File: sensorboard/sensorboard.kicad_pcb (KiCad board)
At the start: 4 copper layers, 100 x 50 mm, 244 parts, among them J1 Conn_01x03, J10 Conn_01x02_Male, J11 Conn_01x05_Male, J12 Conn_01x03, J13 Conn_01x03, J14 USB_C_Receptacle_USB2.0, J2 Conn_01x03, J3 Conn_01x03, J4 Conn_01x03, J5 Conn_01x03, J6 Conn_01x03, J7 Conn_01x03, J8 Conn_01x03, J9 Conn_01x02_Male, Q1 MMDT2222A, U1 ESP32-PICO-D4, U10 MAX31856, U11 MAX31856, U12 RT9025-25GSP, U13 ADS1219, U14 ADS1219, U15 ADS1219, U16 MAX31856, U17 MAX31856, U18 MAX31856, U19 LTC4411, U2 LTC4411, U20 SN65HVD230, U3 TPS61092RSAR, U4 MAX31856, U5 MAX31856, U6 MAX31856, U7 MAX31856, U8 CP2102-GMR-QFN28, U9 MAX31856

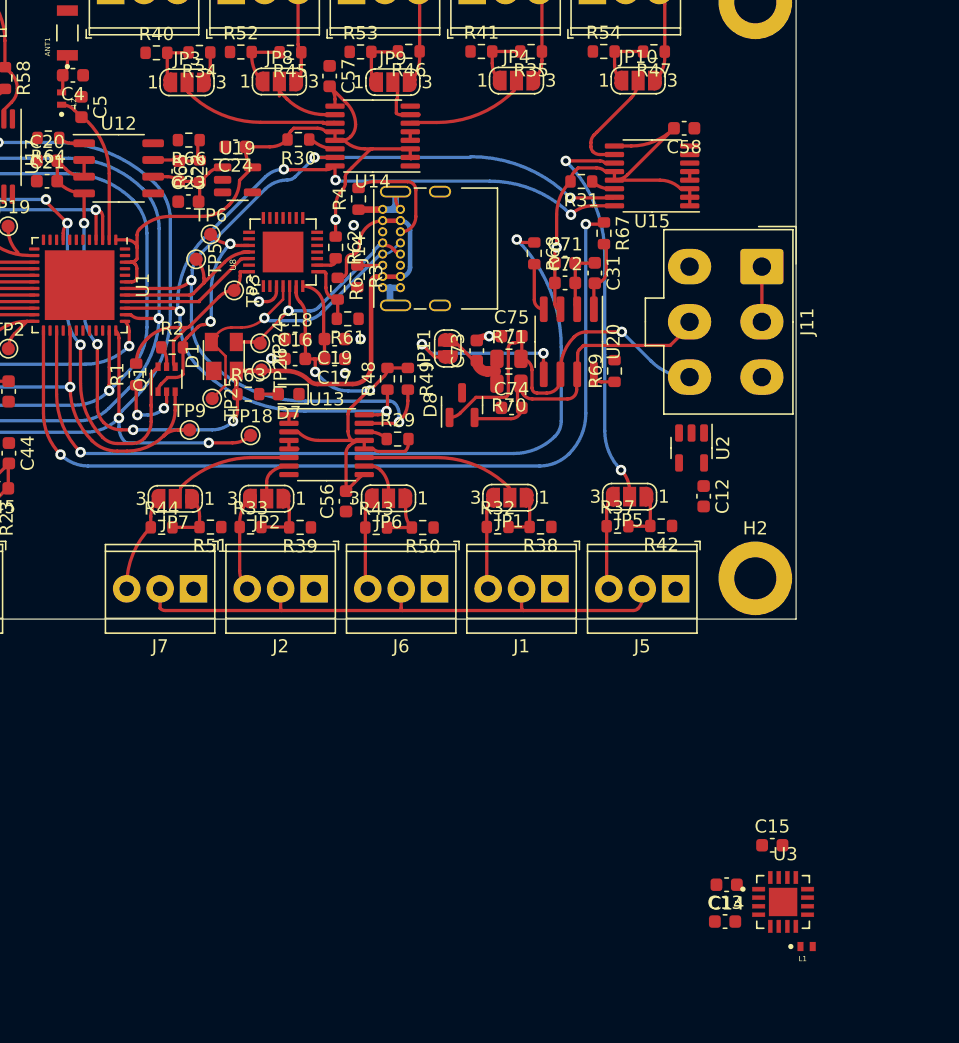
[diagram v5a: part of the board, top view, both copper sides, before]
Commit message: rearrange CAN, USB port and new copies
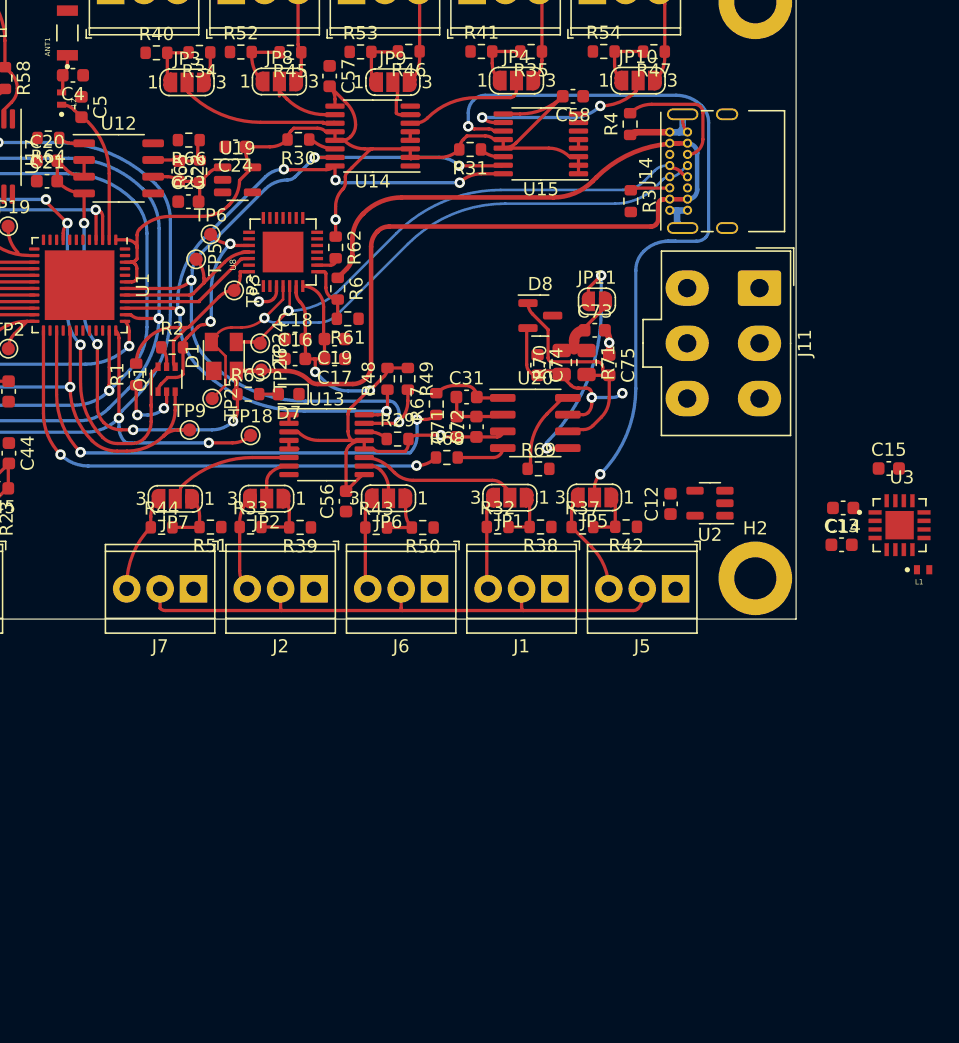
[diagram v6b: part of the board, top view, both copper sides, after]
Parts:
- moved C13 30.0 mm to (203.5, 74.3)
- moved C14 30.0 mm to (203.6, 71.5)
- moved C15 30.0 mm to (207.1, 68.5)
- moved U3 30.0 mm to (207.9, 72.9)
- moved L1 30.0 mm to (209.7, 76.2)
- moved J14 22.6 mm to (190.4, 48.9)
- moved R3 21.6 mm to (187.4, 48.2)
- moved R4 21.4 mm to (187.4, 42.4)
- moved R67 18.2 mm to (172.6, 63.6), turned to 90 degrees
- moved R68 16.9 mm to (173.4, 67.7), turned to 0 degrees
- moved C71 14.9 mm to (174.2, 65.4), turned to 90 degrees
- moved C31 13.6 mm to (174.9, 63.1), turned to 0 degrees
- moved C72 12.8 mm to (175.7, 65.4), turned to 90 degrees
- moved JP11 11.9 mm to (184.9, 55.8), turned to 0 degrees
- moved R69 9.42 mm to (180.4, 68.6), turned to 0 degrees
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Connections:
- TP22 pad 1: /CAN_TX -> /CAN_RX
- TP23 pad 1: /CAN_RX -> /CAN_TX
- U1 pad 25: /CAN_TX -> /CAN_RX
- U1 pad 27: /CAN_RX -> /CAN_TX
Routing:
- net VBUS: track 71.8 -> 123.4 mm
- net /CAN_TX: track 68.1 -> 39.3 mm
- net /analogueI2C/AIN8: track 30.5 -> 58.6 mm
- net /CAN_RX: track 63.5 -> 38.7 mm
- net /usb/Data+: track 24.8 -> 49.3 mm
- net /usb/Data-: track 19.4 -> 42.2 mm
- net /CAN_LOW: track 30.6 -> 18.5 mm, vias 1 -> 0
- net /CAN_HIGH: track 22.7 -> 13.4 mm, vias 0 -> 2
- net /SDA: track 72.4 -> 63.3 mm
- net /SCL: track 69.0 -> 60.0 mm
- net /analogueI2C/AIN9: track 8.49 -> 13.9 mm, vias 0 -> 2
- net Net-(R69-Pad1): track 1.88 -> 6.64 mm
- net /CAN/Vref: track 13.5 -> 17.7 mm
- net GND: track 25.5 -> 21.6 mm, vias 6 -> 2
- net Net-(J5-Pad3): track 7.16 -> 8.45 mm
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
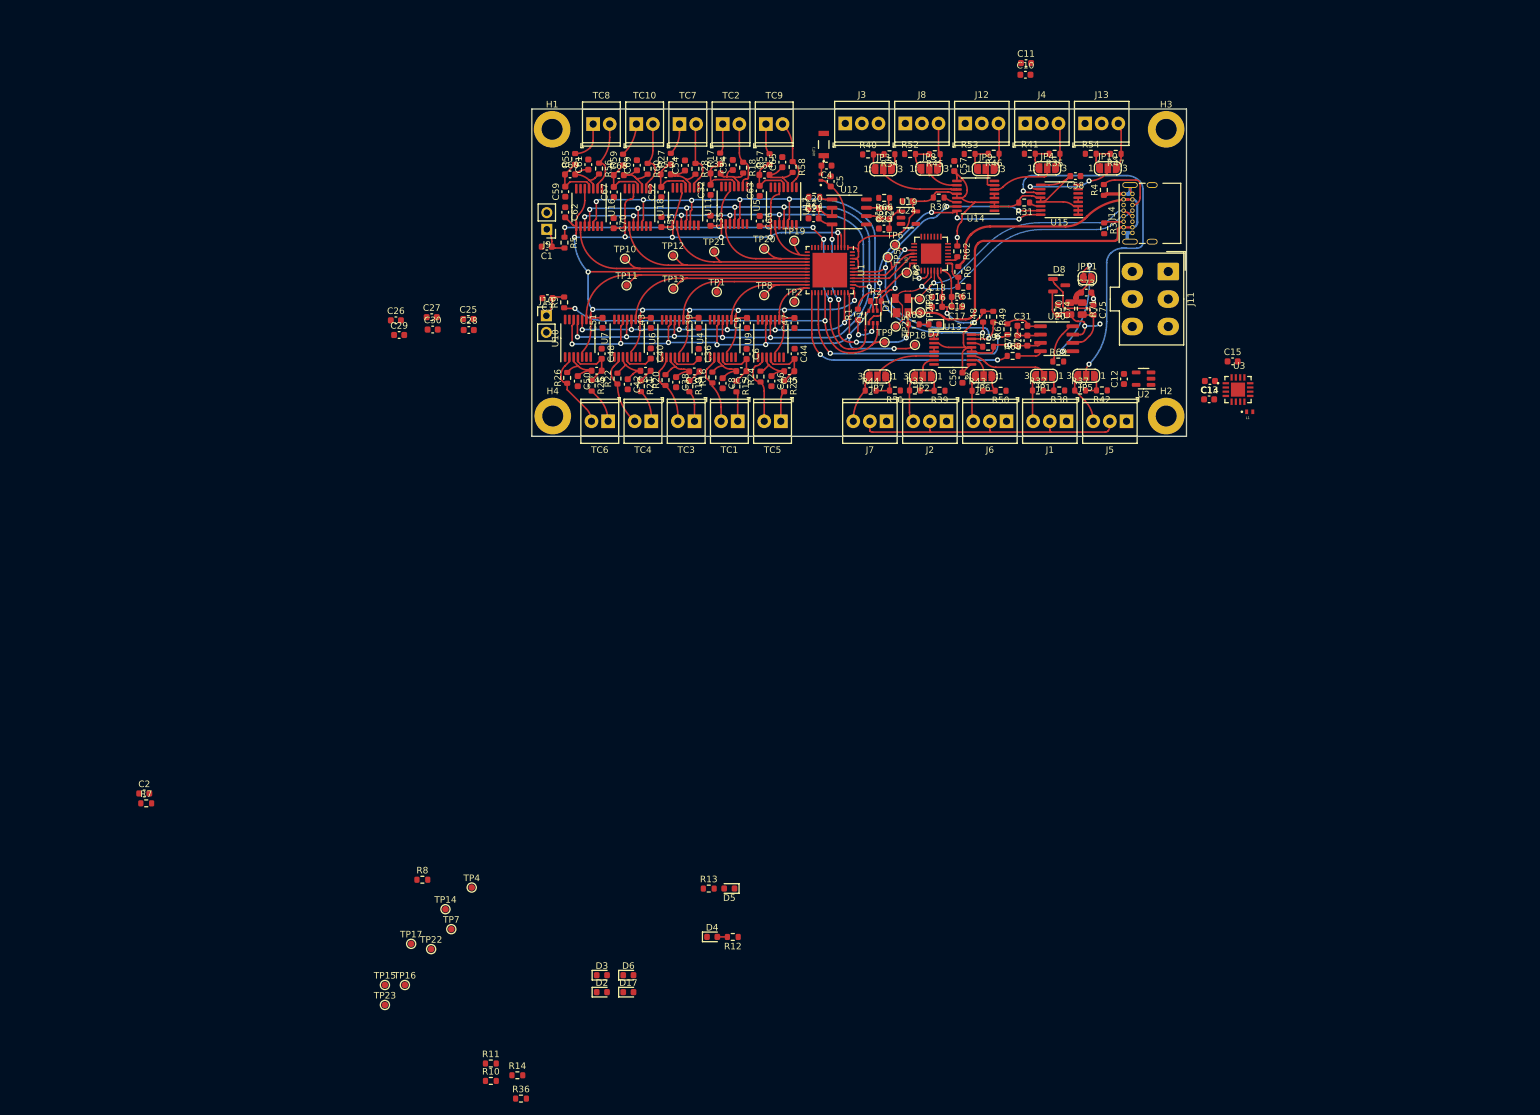
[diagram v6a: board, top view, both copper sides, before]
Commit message: LEDs and repositioning for 5V
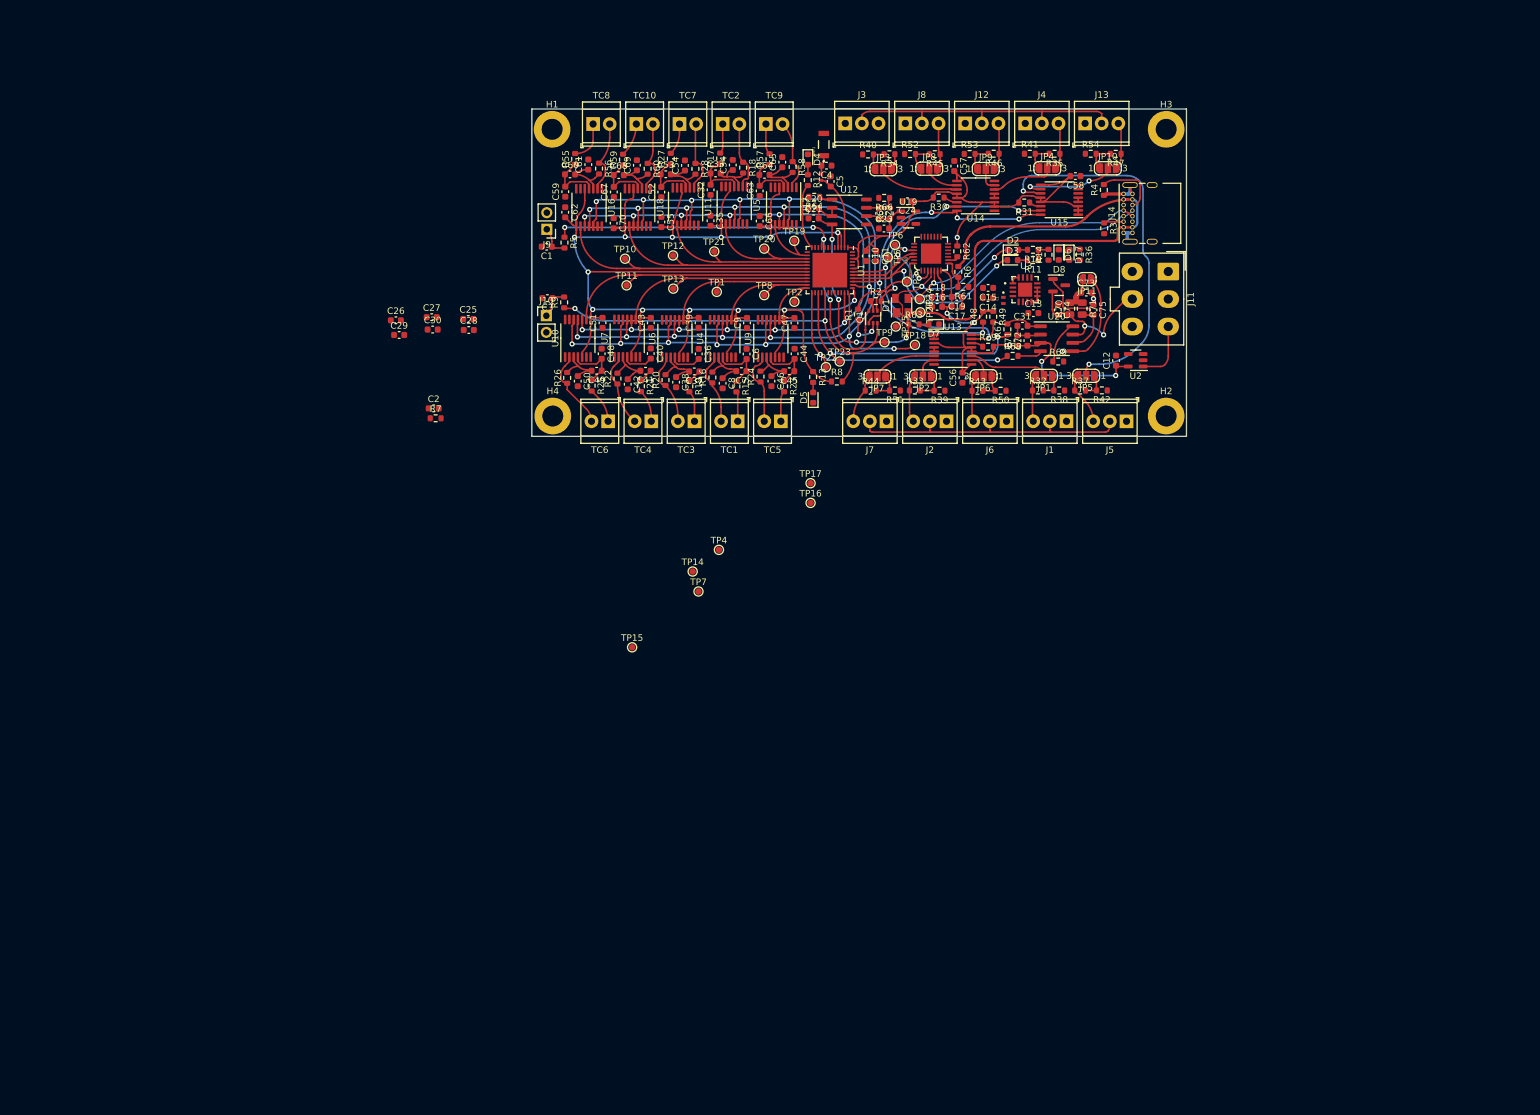
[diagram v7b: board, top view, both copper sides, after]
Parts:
- moved R36 154.6 mm to (183.7, 52.2), turned to -90 degrees
- moved R10 151.6 mm to (176.5, 51.5), turned to 180 degrees
- moved R14 149.3 mm to (178.9, 52.3), turned to 90 degrees
- moved R11 148.0 mm to (176.5, 53.1), turned to 180 degrees
- moved D17 131.2 mm to (182.1, 52.3), turned to -90 degrees
- moved D2 129.6 mm to (173.5, 51.5)
- moved D6 128.2 mm to (180.5, 52.3), turned to -90 degrees
- moved D3 126.0 mm to (173.4, 53.1)
- moved TP23 120.4 mm to (147.0, 68.6)
- moved D4 119.6 mm to (142.2, 37.7), turned to -90 degrees
- moved R12 116.2 mm to (142.2, 40.9), turned to 90 degrees
- moved TP22 107.4 mm to (144.9, 69.4)
- moved R8 99.0 mm to (146.6, 71.6)
- moved TP16 96.2 mm to (142.6, 90.2)
- moved TP17 93.1 mm to (142.6, 87.2)
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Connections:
- C13 pad 1: unconnected-(C13-Pad1) -> +3V3
- C15 pad 1: unconnected-(C15-Pad1) -> +5V
- U1 pad 12: unconnected-(U1-Pad12) -> /LED
- U1 pad 34: /LED -> unconnected-(U1-Pad34)
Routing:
- net +3V3: track 353.8 -> 402.3 mm, vias 17 -> 19
- net +5V: track 44.5 -> 91.2 mm
- net /RXD: track 13.1 -> 38.2 mm, vias 0 -> 2
- net /TXD: track 10.7 -> 34.3 mm, vias 0 -> 2
- net /LED: track 0.00 -> 10.0 mm
- net Net-(J11-Pad3): track 0.00 -> 9.34 mm
- net /CAN_HIGH: track 13.4 -> 21.7 mm
- net /BOOT: track 60.8 -> 65.6 mm
- net GND: track 21.6 -> 24.6 mm
- net /CAN_RX: track 38.7 -> 40.9 mm
- net /CAN_TX: track 39.3 -> 41.2 mm
- net /RTS: track 17.1 -> 19.0 mm
- net /CAN/Vref: track 17.7 -> 15.9 mm, vias 2 -> 1
- net Net-(D5-Pad2): track 0.00 -> 1.54 mm
- net Net-(D3-Pad2): track 0.00 -> 1.51 mm
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
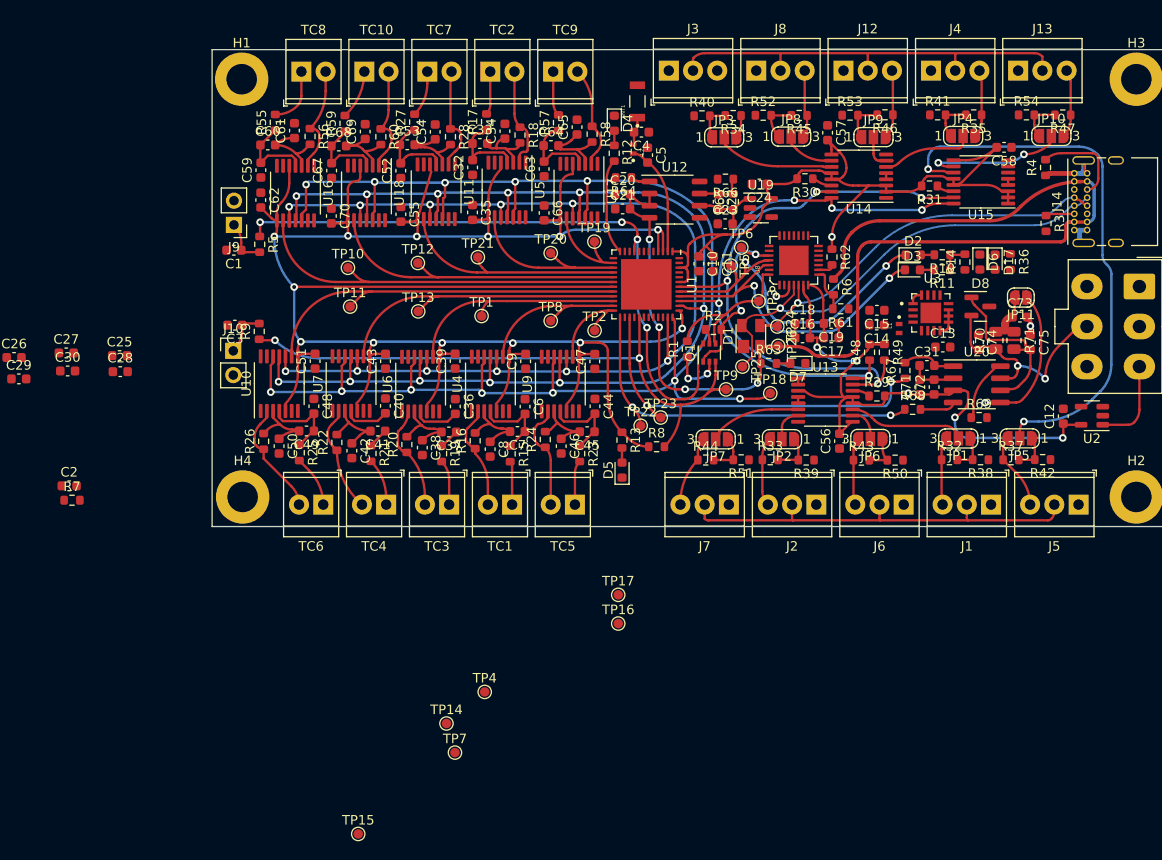
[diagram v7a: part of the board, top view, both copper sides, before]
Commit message: remaining testpoints
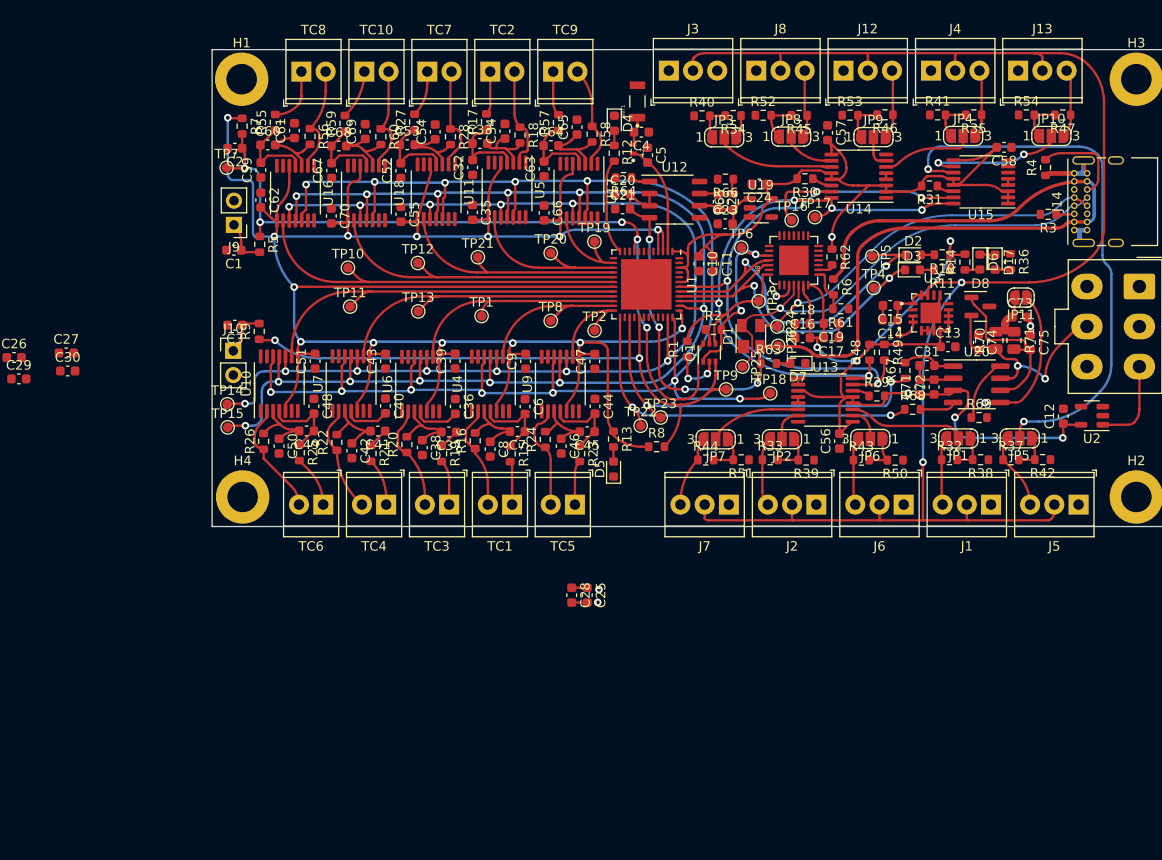
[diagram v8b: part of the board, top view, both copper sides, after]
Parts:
- moved TP7 65.8 mm to (101.5, 42.4)
- moved TP4 58.8 mm to (169.4, 55.0)
- moved C25 55.1 mm to (139.3, 87.2), turned to -90 degrees
- moved C28 52.8 mm to (137.7, 87.2), turned to -90 degrees
- moved TP16 46.0 mm to (160.8, 47.9)
- moved TP15 44.8 mm to (101.6, 69.6)
- moved TP17 44.6 mm to (163.2, 47.6)
- moved R7 43.1 mm to (103.1, 38.0), turned to -90 degrees
- moved TP14 40.6 mm to (101.6, 67.2)
- moved C2 39.4 mm to (102.4, 40.3), turned to 180 degrees
- moved TP5 14.9 mm to (169.2, 51.7)
- moved C14 1.49 mm to (171.1, 58.4)
- moved C15 1.49 mm to (171.1, 56.8)
- moved L1 1.18 mm to (172.0, 60.4)
- moved R3 0.98 mm to (187.7, 47.3), turned to 180 degrees
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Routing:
- net +5V: track 91.2 -> 166.5 mm, vias 0 -> 2
- net +3V3: track 402.3 -> 448.7 mm, vias 19 -> 21
- net /EN: track 70.2 -> 82.6 mm, vias 4 -> 5
- net GND: track 24.6 -> 34.8 mm
- net /MISO: track 131.5 -> 140.7 mm, vias 11 -> 12
- net /SCLK: track 119.9 -> 128.8 mm, vias 11 -> 12
- net /SDA: track 64.3 -> 70.6 mm
- net Net-(L1-Pad2): track 0.00 -> 2.96 mm
- net /SCL: track 60.6 -> 62.7 mm
- net /TXD: track 34.3 -> 36.3 mm
- net /RXD: track 38.2 -> 39.8 mm
- net Net-(D17-Pad2): track 0.00 -> 1.60 mm
- net Net-(D6-Pad2): track 0.00 -> 1.58 mm
- net VBUS: track 123.4 -> 122.3 mm
- net Net-(J14-PadA5): track 3.01 -> 1.92 mm
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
